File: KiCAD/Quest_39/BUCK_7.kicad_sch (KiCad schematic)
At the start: 33 parts, among them U32 AD626ANZ, U33 INA226, U34 LTM4611EV-PBF, U35 MCP4151-502E/SN

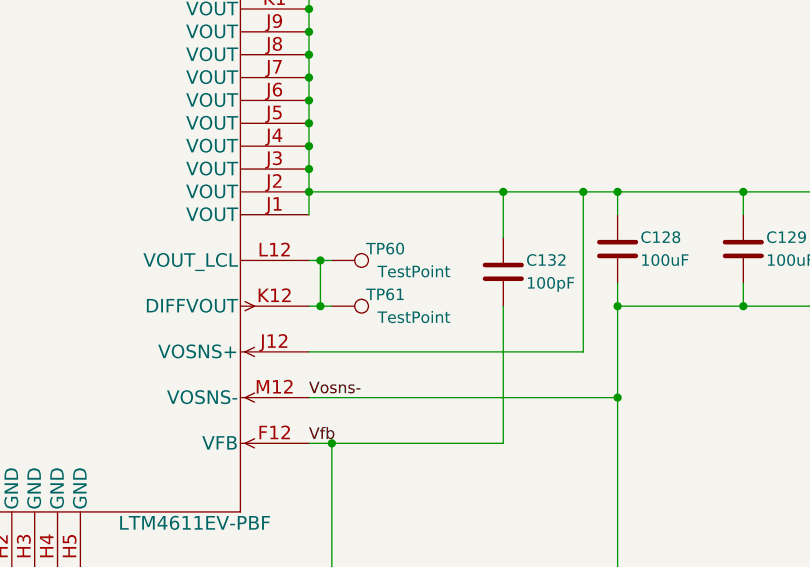
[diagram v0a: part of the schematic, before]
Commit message: Added 3rd buck converter section
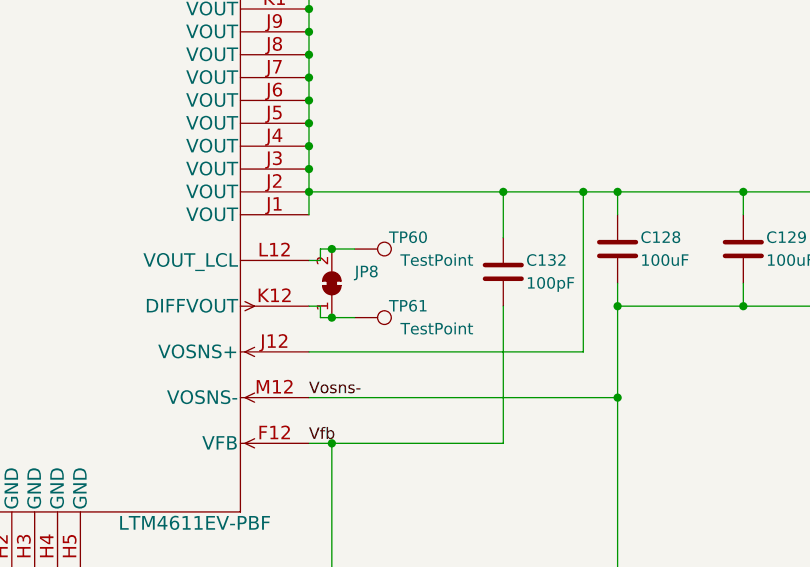
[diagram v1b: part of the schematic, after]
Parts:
- added JP8: SolderJumper_2_Bridged, Jumper:SolderJumper-2_P1.3mm_Bridged_RoundedPad1.0x1.5mm, symbol Jumper:SolderJumper_2_Bridged
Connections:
- net at TP61.1, U34.K12 (DIFFVOUT): now also JP8.1 (A); no longer TP60.1, U34.L12 (VOUT_LCL)
- new net: JP8.2 (B), TP60.1, U34.L12 (VOUT_LCL)
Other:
- moved on the sheet: TP60, TP61

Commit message: Redid layout for the LTM4611EV Buck-converters (Issues with net-assignment to IC pads)
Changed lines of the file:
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@@
   (symbol (lib_id "Device:C") (at 63.5 81.28 0) (unit 1)
     (in_bom yes) (on_board yes)
-    (property "Reference" "C126" (id 0) (at 57.15 80.01 0)
+    (property "Reference" "C126" (id 0) (at 55.88 80.01 0)
       (effects (font (size 1.27 1.27)) (justify left))
     )
@@
   (symbol (lib_id "Device:R") (at 82.55 49.53 0) (unit 1)
     (in_bom yes) (on_board yes)
-    (property "Reference" "R68" (id 0) (at 78.74 48.26 0)
+    (property "Reference" "R68" (id 0) (at 77.47 48.26 0)
       (effects (font (size 1.27 1.27)) (justify left))
     )

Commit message: Added all the SolidWorks files, edited README
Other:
- title: (none) -> BUCK_7
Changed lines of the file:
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@@
 (kicad_sch (version 20211123) (generator eeschema)
   (paper "A3")
+  (title_block
+    (title "BUCK_7")
+    (date "2023-01-31")
+    (rev "1.0")
+  )
   (junction (at 274.32 201.93) (diameter 0) (color 0 0 0 0)
   )
